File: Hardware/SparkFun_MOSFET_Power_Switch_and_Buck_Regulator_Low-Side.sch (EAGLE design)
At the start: 41 parts, among them J1 PTH, J3 5.5x2.1mm Barrel, J4 SMD, Q1 600mA/40V, Q2 100A/100V/6.8mΩ, U1 LMR14203

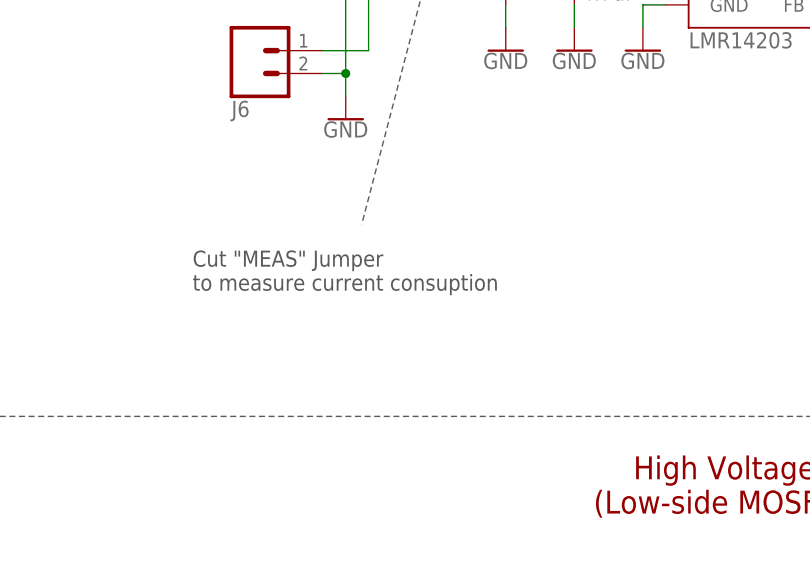
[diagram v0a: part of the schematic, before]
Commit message: Fix minor spelling error in schematic's note. =)
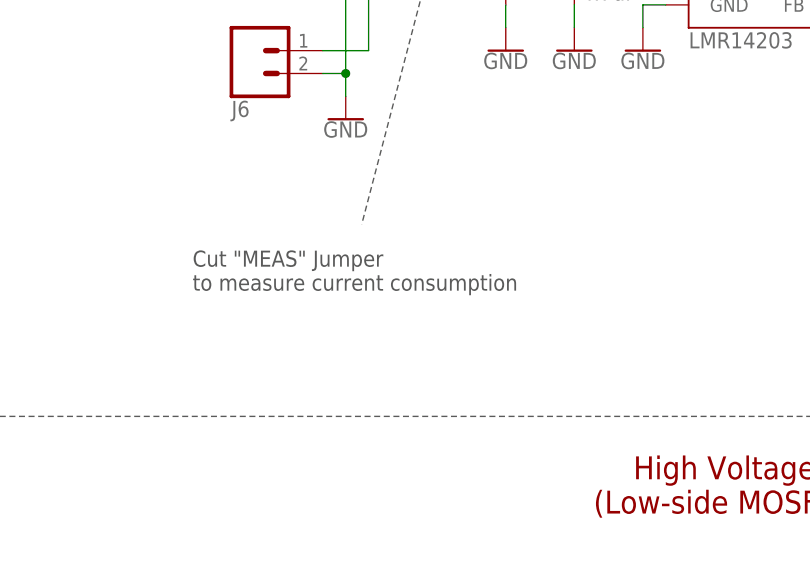
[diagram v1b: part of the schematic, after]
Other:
- note added: "Cut "MEAS" Jumper to measure current consumption"
- note removed: "Cut "MEAS" Jumper to measure current consuption"
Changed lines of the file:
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@@
 <text x="232.156" y="131.572" size="1.778" layer="97" font="vector" rot="R180">(DNP)</text>
 <text x="26.162" y="120.65" size="1.778" layer="97" font="vector">Cut "MEAS" Jumper
-to measure current consuption</text>
+to measure current consumption</text>
 <wire x1="53.34" y1="160.02" x2="44.958" y2="128.016" width="0.1524" layer="97" style="shortdash"/>
 </plain>

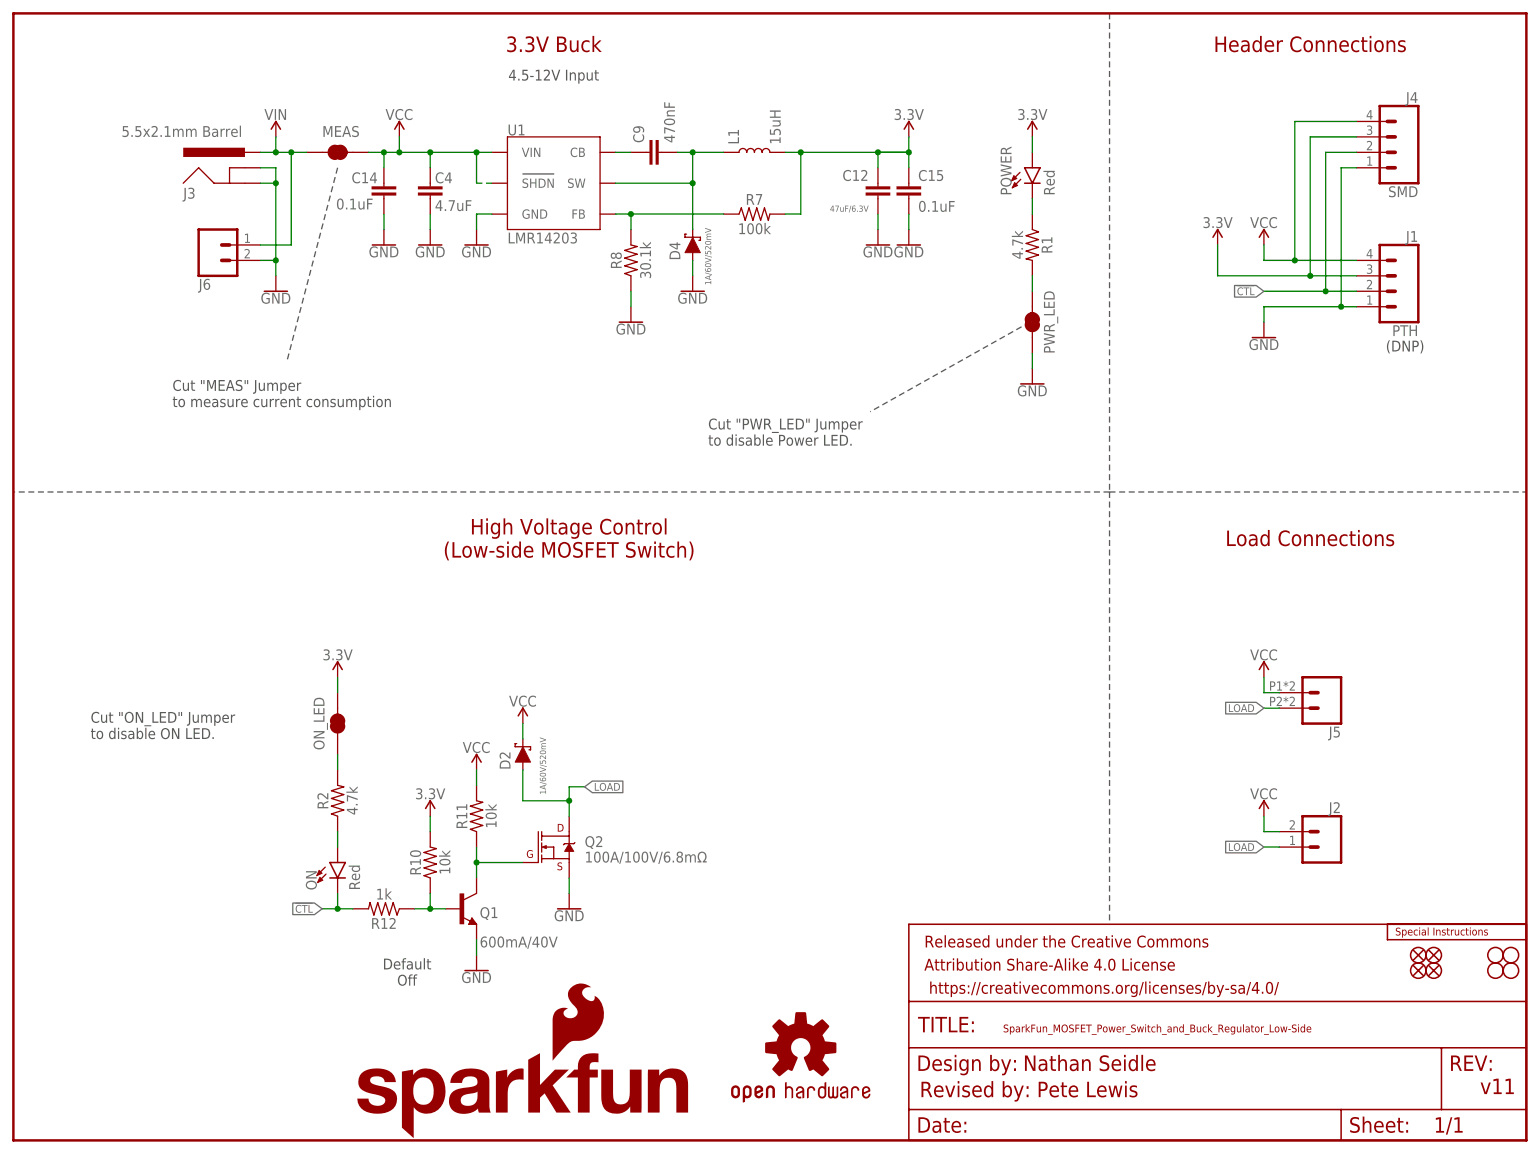
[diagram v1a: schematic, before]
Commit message: updated Q1 and R11
-Q1 is now an NCH MOSFET
-R11 is increased to 100K to save power when things are turned off.
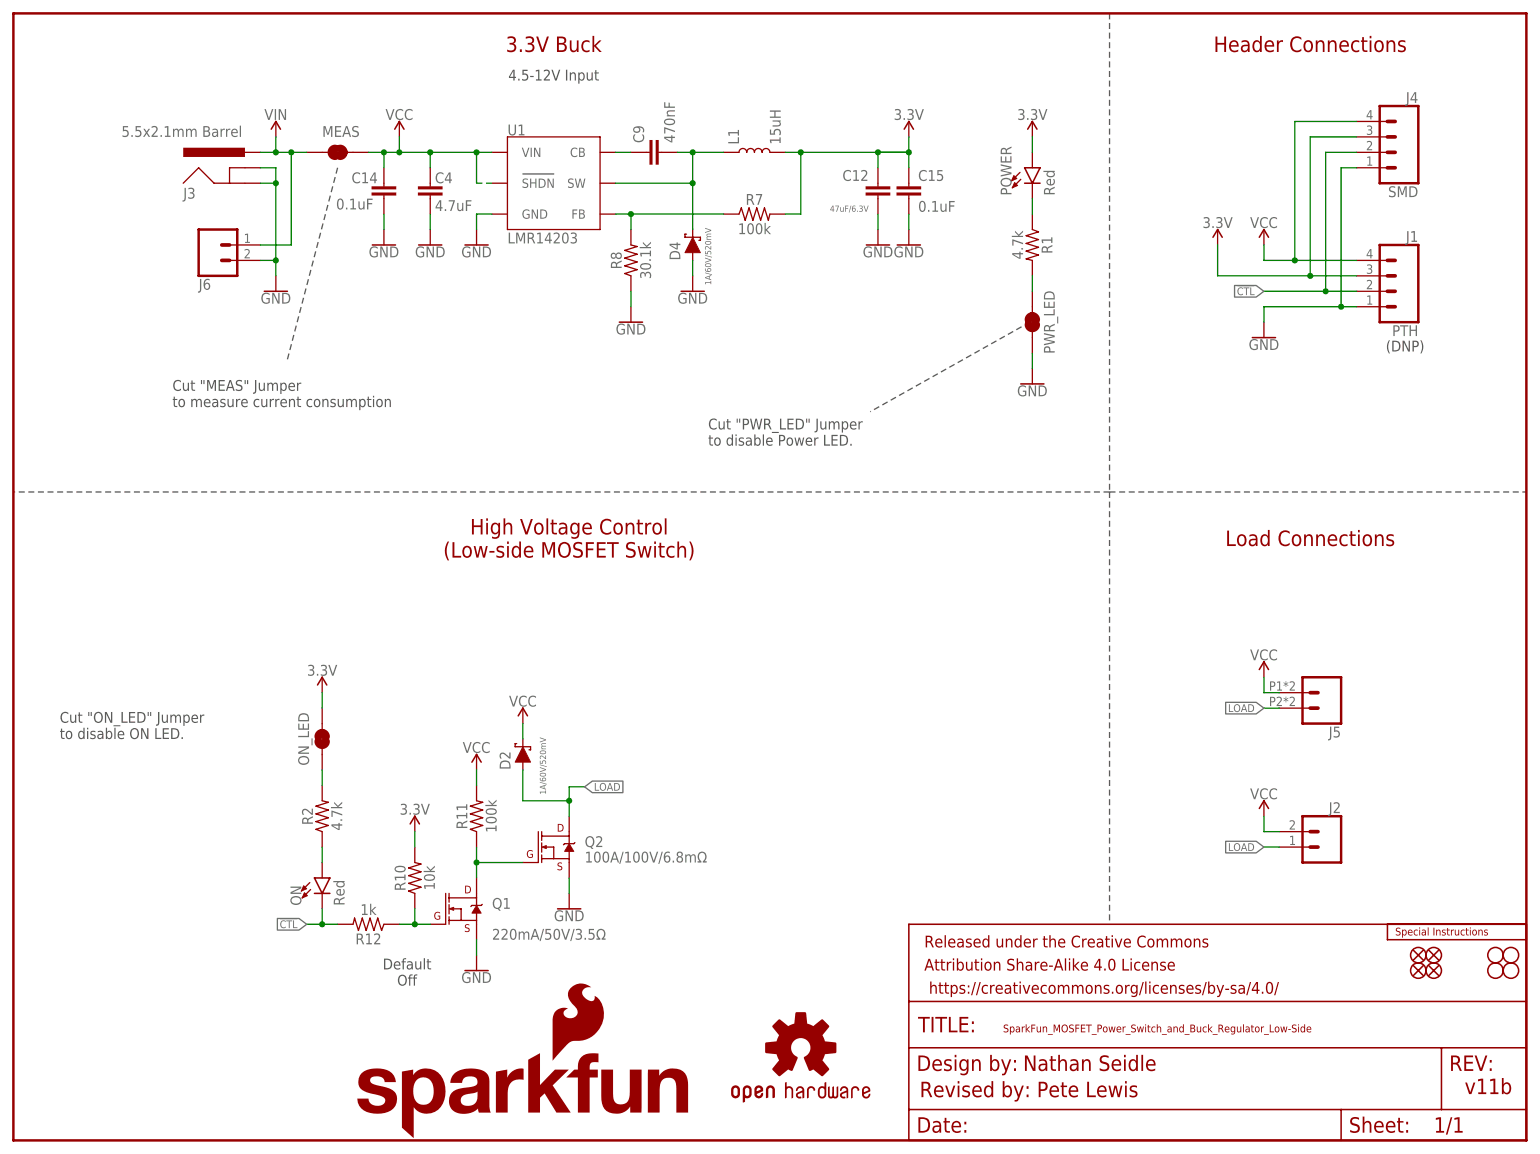
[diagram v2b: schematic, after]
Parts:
- Q1: value 600mA/40V -> 220mA/50V/3.5Ω; device SparkFun-DiscreteSemi:TRANS_NPN-MMBT2222AL -> SparkFun-DiscreteSemi:MOSFET-NCH-BSS138
- R11: value 10k -> 100k; device SparkFun-Resistors:10KOHM-0603-1/10W-1% -> SparkFun-Resistors:100KOHM-0603-1/10W-1%
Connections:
- net GND: now also Q1.S; no longer Q1.E
- net N$1: now also Q1.D; no longer Q1.C
- net N$12: now also Q1.G; no longer Q1.B
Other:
- note added: "v11b"
- note removed: "v11"
- moved on the sheet: ON, ON_LED, R10, R12, R2
